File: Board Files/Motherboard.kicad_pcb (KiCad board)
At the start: 2 copper layers, 196.3 x 118.7 mm, 104 parts, among them P1 72-Pin Connector, P2 EXP-Connector, P3 MOD RF, P4 Controller Input, P5 Controller Input, P6 PWR/RST IN, P8 PWR/RST IN, Q1 2SA937, Q2 2SC2021, Q3 2SC2021, U1 6116 (WRAM), U10 CIC, U2 74HC373, U3 74HC139, U4 6116 (VRAM), U5 RP2C02 PPU, U6 RP2A03 CPU, U7 40H368 (CI), U8 40H368 (CII), U9 74LS04, X1 21.477272 MHz, X2 4MHz

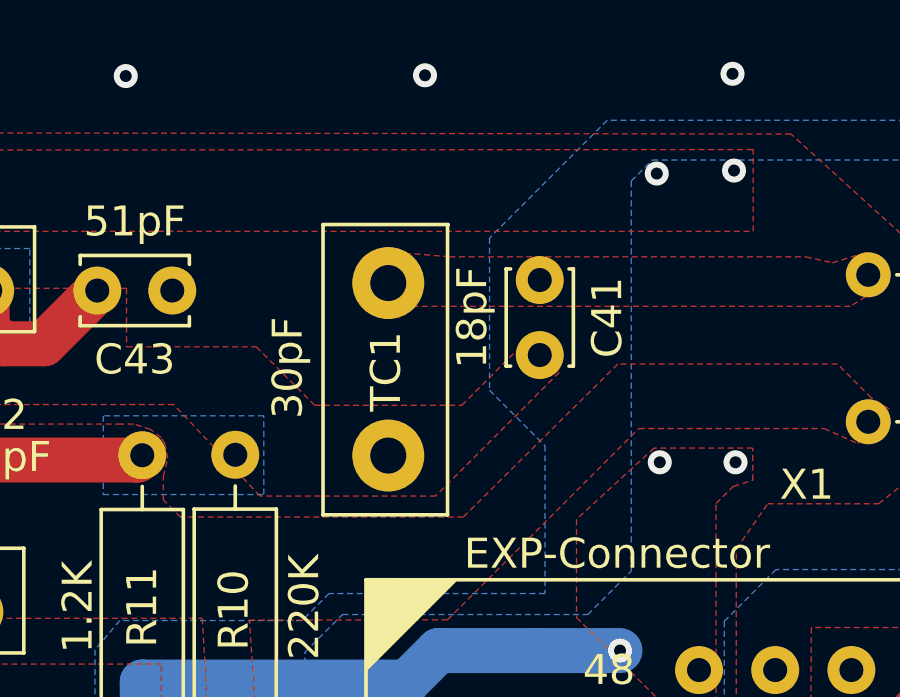
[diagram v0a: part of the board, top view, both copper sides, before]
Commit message: feat: updated trimmer cap footprint
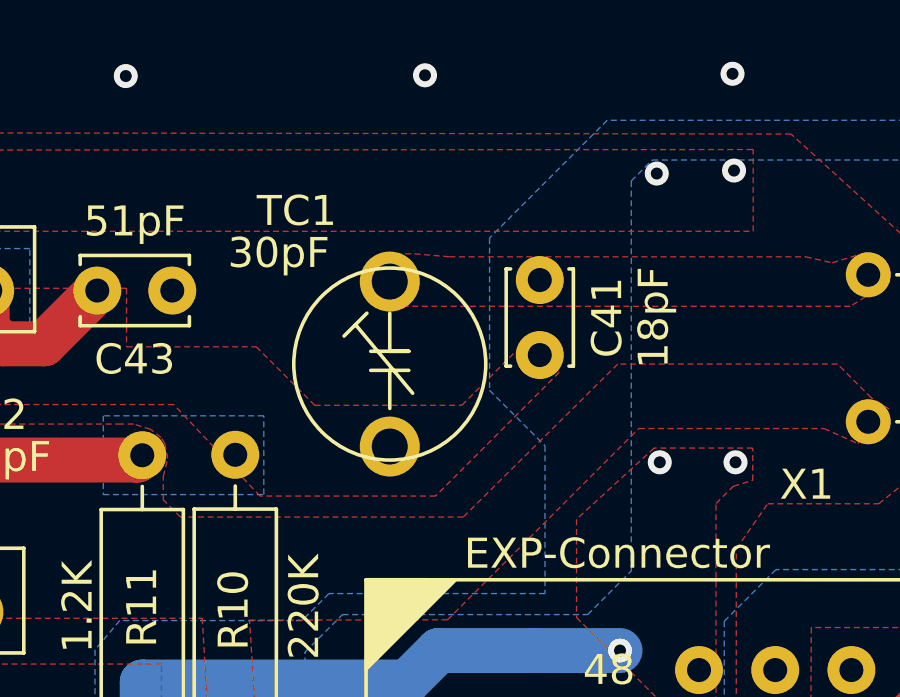
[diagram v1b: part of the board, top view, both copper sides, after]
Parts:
- TC1: footprint NESRE:TrimmerCap-THT -> NESRE:Trimmer_Cap_THT_5_5
- moved TC1 2.07 mm to (82.2, 49.6)
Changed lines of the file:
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@@
 		)
 		(property "Value" "18pF"
-			(at 1.25 2.25 90)
+			(at 1.25 -3.8 90)
 			(layer "F.SilkS")
 			(effects
@@
 		)
 	)
-	(footprint "NESRE:TrimmerCap-THT"
+	(footprint "NESRE:Trimmer_Cap_THT_5_5"
 		(layer "F.Cu")
-		(at 80.15 49.925 90)
+		(at 82.2 49.625 90)
 		(property "Reference" "TC1"
-			(at 2.8 1.925 90)
+			(at 7.85 -3.1 180)
 			(layer "F.SilkS")
 			(effects
@@
 		)
 		(property "Value" "30pF"
-			(at 2.925 -1.35 90)
+			(at 6.45 -3.7 180)
 			(layer "F.SilkS")
 			(effects
@@
 		(property "Datasheet" ""
 			(at 0 0 90)
-			(unlocked yes)
 			(layer "F.Fab")
 			(hide yes)
@@
 		(property "Description" ""
 			(at 0 0 90)
-			(unlocked yes)
 			(layer "F.Fab")
 			(hide yes)
@@
 		(sheetfile "Motherboard.kicad_sch")
 		(attr through_hole)
+		(fp_line
+			(start 3.683 -1.524)
+			(end 4.445 -0.762)
+			(stroke
+				(width 0.12)
+				(type solid)
+			)
+			(layer "F.SilkS")
+		)
+		(fp_line
+			(start 3.175 -0.635)
+			(end 3.175 0.635)
+			(stroke
+				(width 0.12)
+				(type solid)
+			)
+			(layer "F.SilkS")
+		)
+		(fp_line
+			(start 2.54 -0.635)
+			(end 2.54 0.635)
+			(stroke
+				(width 0.12)
+				(type solid)
+			)
+			(layer "F.SilkS")
+		)
+		(fp_line
+			(start 3.175 0)
+			(end 4.445 0)
+			(stroke
+				(width 0.12)
+				(type solid)
+			)
+			(layer "F.SilkS")
+		)
+		(fp_line
+			(start 1.27 0)
+			(end 2.54 0)
+			(stroke
+				(width 0.12)
+				(type solid)
+			)
+			(layer "F.SilkS")
+		)
+		(fp_line
+			(start 3.175 0.635)
+			(end 3.175 0)
+			(stroke
+				(width 0.12)
+				(type solid)
+			)
+			(layer "F.SilkS")
+		)
+		(fp_line
+			(start 1.778 0.762)
+			(end 4.064 -1.143)
+			(stroke
+				(width 0.12)
+				(type solid)
+			)
+			(layer "F.SilkS")
+		)
+		(fp_circle
+			(center 2.75 0)
+			(end 5.95 0)
+			(stroke
+				(width 0.12)
+				(type solid)
+			)
+			(fill no)
+			(layer "F.SilkS")
+		)
 		(pad "1" thru_hole circle
-			(at 0 2 90)
-			(size 2.4 2.4)
+			(at 0 0 90)
+			(size 2 2)
 			(drill 1.2)
 			(layers "*.Cu" "*.Mask")
@@
 		)
 		(pad "2" thru_hole circle
-			(at 5.75 2 90)
-			(size 2.4 2.4)
+			(at 5.5 0 90)
+			(size 2 2)
 			(drill 1.2)
 			(layers "*.Cu" "*.Mask")
@@
 		)
 		(embedded_fonts no)
+		(model "${KIPRJMOD}/Libraries/Trimmer Cap - Green.stp"
+			(offset
+				(xyz 2.6 0 0)
+			)
+			(scale
+				(xyz 1 0.95 1)
+			)
+			(rotate
+				(xyz -0 -0 -90)
+			)
+		)
 	)
 	(footprint "Package_DIP:DIP-20_W7.62mm"
@@
 				"AAAAAAAAAAAAAAAAAAAAAAAAAAAAAAAAAAAAAAAAAAAAAAAAAAAAAAAAAAAAAAAAAAAAAAAAAAAA"
 				"AAAAAAAAAAAAAAAAAAAAAAAAAAAAAAAAAAAAAAAAAAAAAAAAAAAAAAAAAAAAAAAAAAAAAAAAAAAA"
+				"AAAAAAAAAAAAAAAAAAAAAAAAAAAAAAAAAAAAAAAAAAAAAAAAAAAAAAAAAAAAAAAAAAAAAAAAAAAA"
+				"AAAAAAAAAAAAAAAAAAAAAAAAAAAAAAAAAAAAAAAAAAAAAAAAAAAAAAAAAAAAAAAAAAAAAAAAAAAA"
+				"AAAAAAAAAAAAAAAAAAAAAAAAAAAAAAAAAAAAAAAAAAAAAAAAAAAAAAAAAAAAAAAAAAAAAAAAAAAA"
+				"AAAAAAAAAAAAAAAAAAAAAAAAAAAAAAAAAAAAAAAAAAAAAAAAAAAAAAAAAAAAAAAAAAAAAAAAAAAA"
+				"AAAAAAAAAAAAAAAAAAAAAAAAAAAAAAAAAAAAAAAAAAAAAAAAAAAAAAAAAAAAAAAAAAAAAAAAAAAA"
+				"AAAAAAAAAAAAAAAAAAAAAAAAAAAAAAAAAAAAAAAAAAAAAAAAAAAAAAAAAAAAAAAAAAAAAAAAAAAA"
+				"AAAAAAAAAAAAAAAAAAAAAAAAAAAAAAAAAAAAAAAAAAAAAAAAAAAAAAAAAAAAAAAAAAAAAAAAAAAA"
+				"AAAAAAAAAAAAAAAAAAAAAAAAAAAAAAAAAAAAAAAAAAAAAAAAAAAAAAAAAAAAAAAAAAAAAAAAAAAA"
+				"AAAAAAAAAAAAAAAAAAAAAAAAAAAAAAAAAAAAAAAAAAAAAAAAAAAAAAAAAAAAAAAAAAAAAAAAAAAA"
+				"AAAAAAAAAAAAAAAAAAAAAAAAAAAAAAAAAAAAAAAAAAAAAAAAAAAAAAAAAAAAAAAAAAAAAAAAAAAA"
+				"AAAAAAAAAAAAAAAAAAAAAAAAAAAAAAAAAAAAAAAAAAAAAAAAAAAAAAAAAAAAAAAAAAAAAAAAAAAA"
+				"AAAAAAAAAAAAAAAAAAAAAAAAAAAAAAAAAAAAAAAAAAAAAAAAAAAAAAAAAAAAAAAAAAAAAAAAAAAA"
+				"AAAAAAAAAAAAAAAAAAAAAAAAAAAAAAAAAAAAAAAAAAAAAAAAAAAAAAAAAAAAAAAAAAAAAAAAAAAA"
+				"AAAAAAAAAAAAAAAAAAAAAAAAAAAAAAAAAAAAAAAAAAAAAAAAAAAAAAAAAAAAAAAAAAAAAAAAAAAA"
+				"AAAAAAAAAAAAAAAAAAAAAAAAAAAAAAAAAAAAAAAAAAAAAAAAAAAAAAAAAAAAAAAAAAAAAAAAAAAA"
+				"AAAAAAAAAAAAAAAAAAAAAAAAAAAAAAAAAAAAAAAAAAAAAAAAAAAAAAAAAAAAAAAAAAAAAAAAAAAA"
+				"AAAAAAAAAAAAAAAAAAAAAAAAAAAAAAAAAAAAAAAAAAAAAAAAAAAAAAAAAAAAAAAAAAAAAAAAAAAA"
+				"AAAAAAAAAAAAAAAAAAAAAAAAAAAAAAAAAAAAAAAAAAAAAAAAAAAAAAAAAAAAAAAAAAAAAAAAAAAA"
 				"AAAAAAAAAAAAAAAAAAAAAAAAAAAAAAAAAAAAAAAAAAAAAA=="
 			)
@@
 		(layer "F.SilkS")
 	)
-	(gr_line
-		(start 79.975 42.225)
-		(end 79.975 51.9)
-		(stroke
-			(width 0.12)
-			(type solid)
-		)
-		(layer "F.SilkS")
-	)
-	(gr_line
-		(start 79.975 51.9)
-		(end 84.125 51.9)
-		(stroke
-			(width 0.12)
-			(type solid)
-		)
-		(layer "F.SilkS")
-	)
 	(gr_circle
 		(center 172.05 106.5)
@@
 	)
 	(gr_line
-		(start 84.15 42.225)
-		(end 79.975 42.225)
-		(stroke
-			(width 0.12)
-			(type solid)
-		)
-		(layer "F.SilkS")
-	)
-	(gr_line
 		(start 198.375 110.625)
 		(end 198.375 110.825)
@@
 		)
 		(layer "F.SilkS")
-	)
-	(gr_line
-		(start 84.125 51.9)
-		(end 84.125 42.225)
-		(stroke
-			(width 0.12)
-			(type solid)
-		)
-		(layer "F.SilkS")
